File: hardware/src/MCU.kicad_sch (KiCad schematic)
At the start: 0 parts

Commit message: Add: MCU and power supply. And connected to USB in top level schematic
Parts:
- added C201, C205, C207: 10µF, symbol Device:C
- added C202, C204, C206: 0.1µF, symbol Device:C
- added C203: 1µF, symbol Device:C
- added D201, D202: LED, symbol Device:LED
- added R201, R202: 10k, symbol Device:R
- added R203: 300, symbol Device:R
- added R204: 150, symbol Device:R
- added U201: ESP32-C3-WROOM-02, RF_Module:ESP32-C3-WROOM-02, symbol RF_Module:ESP32-C3-WROOM-02
- added U202: TLV1117LV33, symbol Regulator_Linear:TLV1117-33
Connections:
- new net: R201.2, U201.7 (IO8)
- new net: D201.2 (A), R203.2
- new net: D202.2 (A), R204.2
- new net +3V3: C201.1, C202.1, C204.1, C205.1, R201.1, R202.1, R204.1, U201.1 (3V3), U202.2 (VO)
- new net EN: C203.1, R202.2, U201.2 (EN)
- new net GND: C201.2, C202.2, C203.2, C204.2, C205.2, C206.2, C207.2, D201.1 (K), D202.1 (K), U201.19 (GND), U201.9 (GND), U202.1 (GND)
- new net IO0: U201.18 (IO0)
- new net IO1: U201.17 (IO1)
- new net IO10: U201.10 (IO10)
- new net IO18: U201.13 (IO18)
- new net IO19: U201.14 (IO19)
- new net IO3: U201.15 (IO3)
- new net IO4: U201.3 (IO4)
- new net IO5: U201.4 (IO5)
- new net IO6: U201.5 (IO6)
- new net IO7: U201.6 (IO7)
- new net IO9: U201.8 (IO9)
- new net UART.RXD: U201.12 (IO21/TXD)
- new net UART.TXD: U201.11 (IO20/RXD)
- new net VBUS: C206.1, C207.1, R203.1, U202.3 (VI)
- no-connect marks 0 -> 1
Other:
- title: Wordclock - Microcontroller Unit -> Wordclock - Microcontroller Unit & Power Supply

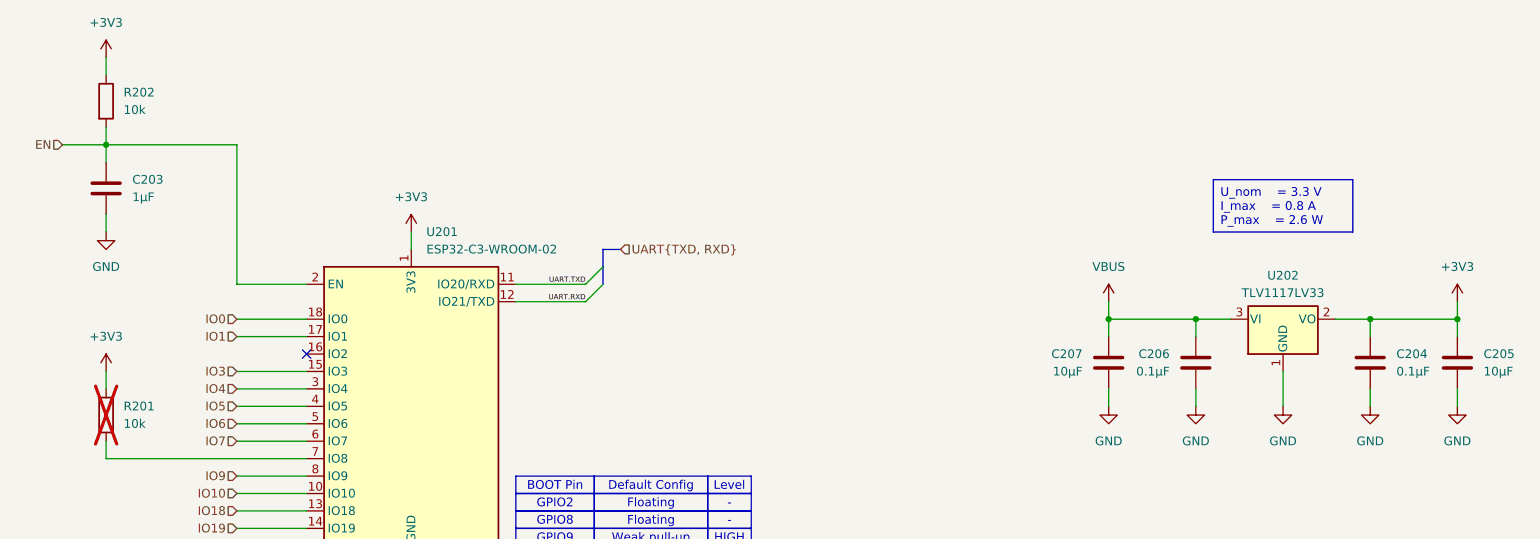
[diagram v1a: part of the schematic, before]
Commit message: Add: LEDs to the schematic
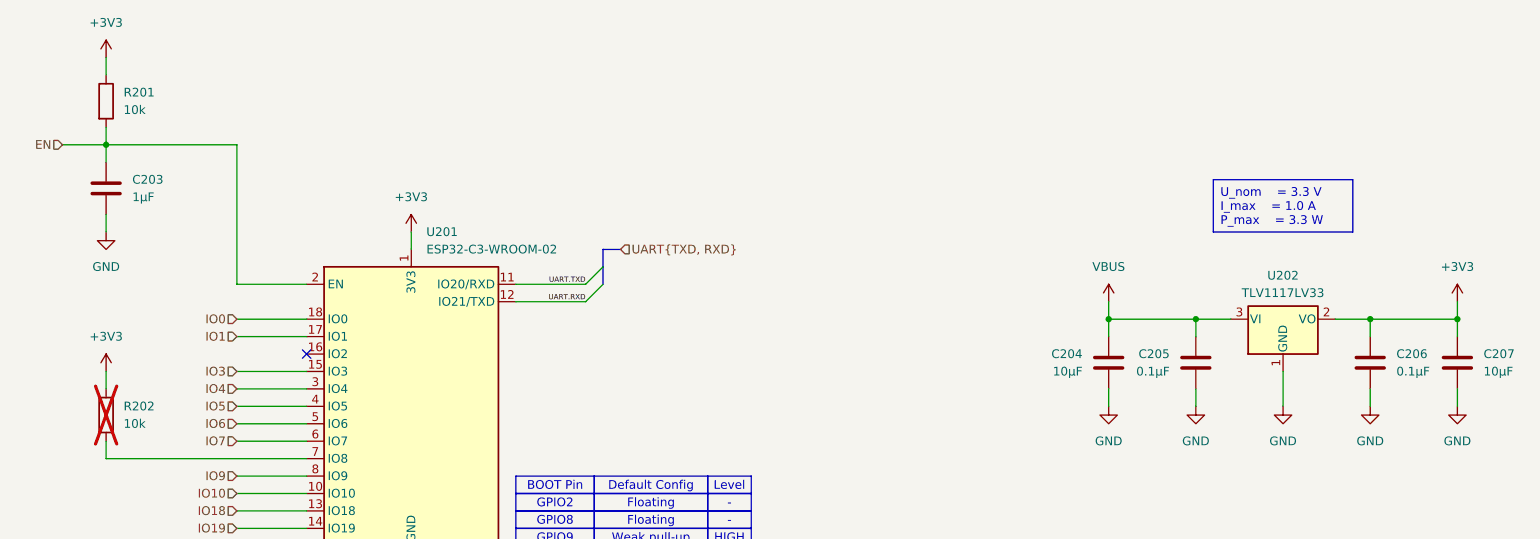
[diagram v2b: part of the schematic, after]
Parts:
- renumbered C207 to C204, C206 to C205, C204 to C206, C205 to C207, R202 to R201, R201 to R202
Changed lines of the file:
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@@
 		)
 	)
-	(text_box "U_nom	= 3.3 V\nI_max	= 0.8 A\nP_max	= 2.6 W"
+	(text_box "U_nom	= 3.3 V\nI_max	= 1.0 A\nP_max	= 3.3 W"
 		(exclude_from_sim no)
 		(at 205.74 43.18 0)
@@
 		(dnp no)
 		(fields_autoplaced yes)
-		(property "Reference" "#PWR0213"
+		(property "Reference" "#PWR0216"
 			(at 228.6 82.55 0)
 			(effects
@@
 			(project "ESP-Wordclock"
 				(path "/bfaac094-0365-40a4-8b7a-d4d62ace544e/148425c6-8949-47fb-990d-0e511c74cf4c"
-					(reference "#PWR0213")
+					(reference "#PWR0216")
 					(unit 1)
 				)
@@
 		(dnp no)
 		(fields_autoplaced yes)
-		(property "Reference" "#PWR0208"
+		(property "Reference" "#PWR0205"
 			(at 44.45 29.21 0)
 			(effects
@@
 			(project "ESP-Wordclock"
 				(path "/bfaac094-0365-40a4-8b7a-d4d62ace544e/148425c6-8949-47fb-990d-0e511c74cf4c"
-					(reference "#PWR0208")
+					(reference "#PWR0205")
 					(unit 1)
 				)
@@
 		(dnp no)
 		(fields_autoplaced yes)
-		(property "Reference" "#PWR0209"
+		(property "Reference" "#PWR0206"
 			(at 44.45 57.15 0)
 			(effects
@@
 			(project ""
 				(path "/bfaac094-0365-40a4-8b7a-d4d62ace544e/148425c6-8949-47fb-990d-0e511c74cf4c"
-					(reference "#PWR0209")
+					(reference "#PWR0206")
 					(unit 1)
 				)
@@
 		(dnp no)
 		(fields_autoplaced yes)
-		(property "Reference" "C205"
+		(property "Reference" "C207"
 			(at 245.11 68.5799 0)
 			(effects
@@
 			(project "ESP-Wordclock"
 				(path "/bfaac094-0365-40a4-8b7a-d4d62ace544e/148425c6-8949-47fb-990d-0e511c74cf4c"
-					(reference "C205")
+					(reference "C207")
 					(unit 1)
 				)
@@
 		(dnp no)
 		(fields_autoplaced yes)
-		(property "Reference" "#PWR0216"
+		(property "Reference" "#PWR0219"
 			(at 241.3 64.77 0)
 			(effects
@@
 			(project ""
 				(path "/bfaac094-0365-40a4-8b7a-d4d62ace544e/148425c6-8949-47fb-990d-0e511c74cf4c"
-					(reference "#PWR0216")
+					(reference "#PWR0219")
 					(unit 1)
 				)
@@
 		(dnp no)
 		(fields_autoplaced yes)
-		(property "Reference" "#PWR0220"
+		(property "Reference" "#PWR0218"
 			(at 228.6 146.05 0)
 			(effects
@@
 			(project "ESP-Wordclock"
 				(path "/bfaac094-0365-40a4-8b7a-d4d62ace544e/148425c6-8949-47fb-990d-0e511c74cf4c"
-					(reference "#PWR0220")
+					(reference "#PWR0218")
 					(unit 1)
 				)
@@
 		(dnp no)
 		(fields_autoplaced yes)
-		(property "Reference" "#PWR0202"
+		(property "Reference" "#PWR0209"
 			(at 88.9 107.95 0)
 			(effects
@@
 			(project ""
 				(path "/bfaac094-0365-40a4-8b7a-d4d62ace544e/148425c6-8949-47fb-990d-0e511c74cf4c"
-					(reference "#PWR0202")
+					(reference "#PWR0209")
 					(unit 1)
 				)
@@
 		(on_board yes)
 		(dnp no)
-		(property "Reference" "C206"
+		(property "Reference" "C205"
 			(at 199.39 68.5799 0)
 			(effects
@@
 			(project "ESP-Wordclock"
 				(path "/bfaac094-0365-40a4-8b7a-d4d62ace544e/148425c6-8949-47fb-990d-0e511c74cf4c"
-					(reference "C206")
+					(reference "C205")
 					(unit 1)
 				)
@@
 		(dnp yes)
 		(fields_autoplaced yes)
-		(property "Reference" "R201"
+		(property "Reference" "R202"
 			(at 46.99 76.1999 0)
 			(effects
@@
 			(project ""
 				(path "/bfaac094-0365-40a4-8b7a-d4d62ace544e/148425c6-8949-47fb-990d-0e511c74cf4c"
-					(reference "R201")
+					(reference "R202")
 					(unit 1)
 				)
@@
 		(dnp no)
 		(fields_autoplaced yes)
-		(property "Reference" "#PWR0215"
+		(property "Reference" "#PWR0210"
 			(at 190.5 64.77 0)
 			(effects
@@
 			(project ""
 				(path "/bfaac094-0365-40a4-8b7a-d4d62ace544e/148425c6-8949-47fb-990d-0e511c74cf4c"
-					(reference "#PWR0215")
+					(reference "#PWR0210")
 					(unit 1)
 				)
@@
 		(dnp no)
 		(fields_autoplaced yes)
-		(property "Reference" "#PWR0206"
+		(property "Reference" "#PWR0204"
 			(at 38.1 190.5 0)
 			(effects
@@
 			(project "ESP-Wordclock"
 				(path "/bfaac094-0365-40a4-8b7a-d4d62ace544e/148425c6-8949-47fb-990d-0e511c74cf4c"
-					(reference "#PWR0206")
+					(reference "#PWR0204")
 					(unit 1)
 				)
@@
 		(dnp no)
 		(fields_autoplaced yes)
-		(property "Reference" "#PWR0205"
+		(property "Reference" "#PWR0203"
 			(at 38.1 175.26 0)
 			(effects
@@
 			(project "ESP-Wordclock"
 				(path "/bfaac094-0365-40a4-8b7a-d4d62ace544e/148425c6-8949-47fb-990d-0e511c74cf4c"
-					(reference "#PWR0205")
+					(reference "#PWR0203")
 					(unit 1)
 				)
@@
 		(dnp no)
 		(fields_autoplaced yes)
-		(property "Reference" "#PWR0218"
+		(property "Reference" "#PWR0213"
 			(at 203.2 118.11 0)
 			(effects
@@
 			(project "ESP-Wordclock"
 				(path "/bfaac094-0365-40a4-8b7a-d4d62ace544e/148425c6-8949-47fb-990d-0e511c74cf4c"
-					(reference "#PWR0218")
+					(reference "#PWR0213")
 					(unit 1)
 				)
@@
 		(dnp no)
 		(fields_autoplaced yes)
-		(property "Reference" "#PWR0201"
+		(property "Reference" "#PWR0208"
 			(at 88.9 54.61 0)
 			(effects
@@
 			(project ""
 				(path "/bfaac094-0365-40a4-8b7a-d4d62ace544e/148425c6-8949-47fb-990d-0e511c74cf4c"
-					(reference "#PWR0201")
+					(reference "#PWR0208")
 					(unit 1)
 				)
@@
 		(dnp no)
 		(fields_autoplaced yes)
-		(property "Reference" "#PWR0203"
+		(property "Reference" "#PWR0201"
 			(at 25.4 175.26 0)
 			(effects
@@
 			(project "ESP-Wordclock"
 				(path "/bfaac094-0365-40a4-8b7a-d4d62ace544e/148425c6-8949-47fb-990d-0e511c74cf4c"
-					(reference "#PWR0203")
+					(reference "#PWR0201")
 					(unit 1)
 				)
@@
 		(dnp no)
 		(fields_autoplaced yes)
-		(property "Reference" "#PWR0210"
+		(property "Reference" "#PWR0211"
 			(at 190.5 82.55 0)
 			(effects
@@
 			(project "ESP-Wordclock"
 				(path "/bfaac094-0365-40a4-8b7a-d4d62ace544e/148425c6-8949-47fb-990d-0e511c74cf4c"
-					(reference "#PWR0210")
+					(reference "#PWR0211")
 					(unit 1)
 				)
@@
 		(dnp no)
 		(fields_autoplaced yes)
-		(property "Reference" "R202"
+		(property "Reference" "R201"
 			(at 46.99 30.4799 0)
 			(effects
@@
 			(project "ESP-Wordclock"
 				(path "/bfaac094-0365-40a4-8b7a-d4d62ace544e/148425c6-8949-47fb-990d-0e511c74cf4c"
-					(reference "R202")
+					(reference "R201")
 					(unit 1)
 				)
@@
 		(on_board yes)
 		(dnp no)
-		(property "Reference" "C207"
+		(property "Reference" "C204"
 			(at 186.69 68.5799 0)
 			(effects
@@
 			(project "ESP-Wordclock"
 				(path "/bfaac094-0365-40a4-8b7a-d4d62ace544e/148425c6-8949-47fb-990d-0e511c74cf4c"
-					(reference "C207")
+					(reference "C204")
 					(unit 1)
 				)
@@
 		(dnp no)
 		(fields_autoplaced yes)
-		(property "Reference" "#PWR0204"
+		(property "Reference" "#PWR0202"
 			(at 25.4 190.5 0)
 			(effects
@@
 			(project "ESP-Wordclock"
 				(path "/bfaac094-0365-40a4-8b7a-d4d62ace544e/148425c6-8949-47fb-990d-0e511c74cf4c"
-					(reference "#PWR0204")
+					(reference "#PWR0202")
 					(unit 1)
 				)
@@
 		(dnp no)
 		(fields_autoplaced yes)
-		(property "Reference" "C204"
+		(property "Reference" "C206"
 			(at 232.41 68.5799 0)
 			(effects
@@
 			(project ""
 				(path "/bfaac094-0365-40a4-8b7a-d4d62ace544e/148425c6-8949-47fb-990d-0e511c74cf4c"
-					(reference "C204")
+					(reference "C206")
 					(unit 1)
 				)
@@
 		(dnp no)
 		(fields_autoplaced yes)
-		(property "Reference" "#PWR0211"
+		(property "Reference" "#PWR0212"
 			(at 203.2 82.55 0)
 			(effects
@@
 			(project "ESP-Wordclock"
 				(path "/bfaac094-0365-40a4-8b7a-d4d62ace544e/148425c6-8949-47fb-990d-0e511c74cf4c"
-					(reference "#PWR0211")
+					(reference "#PWR0212")
 					(unit 1)
 				)
@@
 		(dnp no)
 		(fields_autoplaced yes)
-		(property "Reference" "#PWR0219"
+		(property "Reference" "#PWR0214"
 			(at 203.2 146.05 0)
 			(effects
@@
 			(project "ESP-Wordclock"
 				(path "/bfaac094-0365-40a4-8b7a-d4d62ace544e/148425c6-8949-47fb-990d-0e511c74cf4c"
-					(reference "#PWR0219")
+					(reference "#PWR0214")
 					(unit 1)
 				)
@@
 		(dnp no)
 		(fields_autoplaced yes)
-		(property "Reference" "#PWR0212"
+		(property "Reference" "#PWR0215"
 			(at 215.9 82.55 0)
 			(effects
@@
 			(project "ESP-Wordclock"
 				(path "/bfaac094-0365-40a4-8b7a-d4d62ace544e/148425c6-8949-47fb-990d-0e511c74cf4c"
-					(reference "#PWR0212")
+					(reference "#PWR0215")
 					(unit 1)
 				)
@@
 		(dnp no)
 		(fields_autoplaced yes)
-		(property "Reference" "#PWR0214"
+		(property "Reference" "#PWR0220"
 			(at 241.3 82.55 0)
 			(effects
@@
 			(project "ESP-Wordclock"
 				(path "/bfaac094-0365-40a4-8b7a-d4d62ace544e/148425c6-8949-47fb-990d-0e511c74cf4c"
-					(reference "#PWR0214")
-					(unit 1)
-				)
+					(reference "#PWR0220")
+					(unit 1)
+				)
